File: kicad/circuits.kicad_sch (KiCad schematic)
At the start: 28 parts

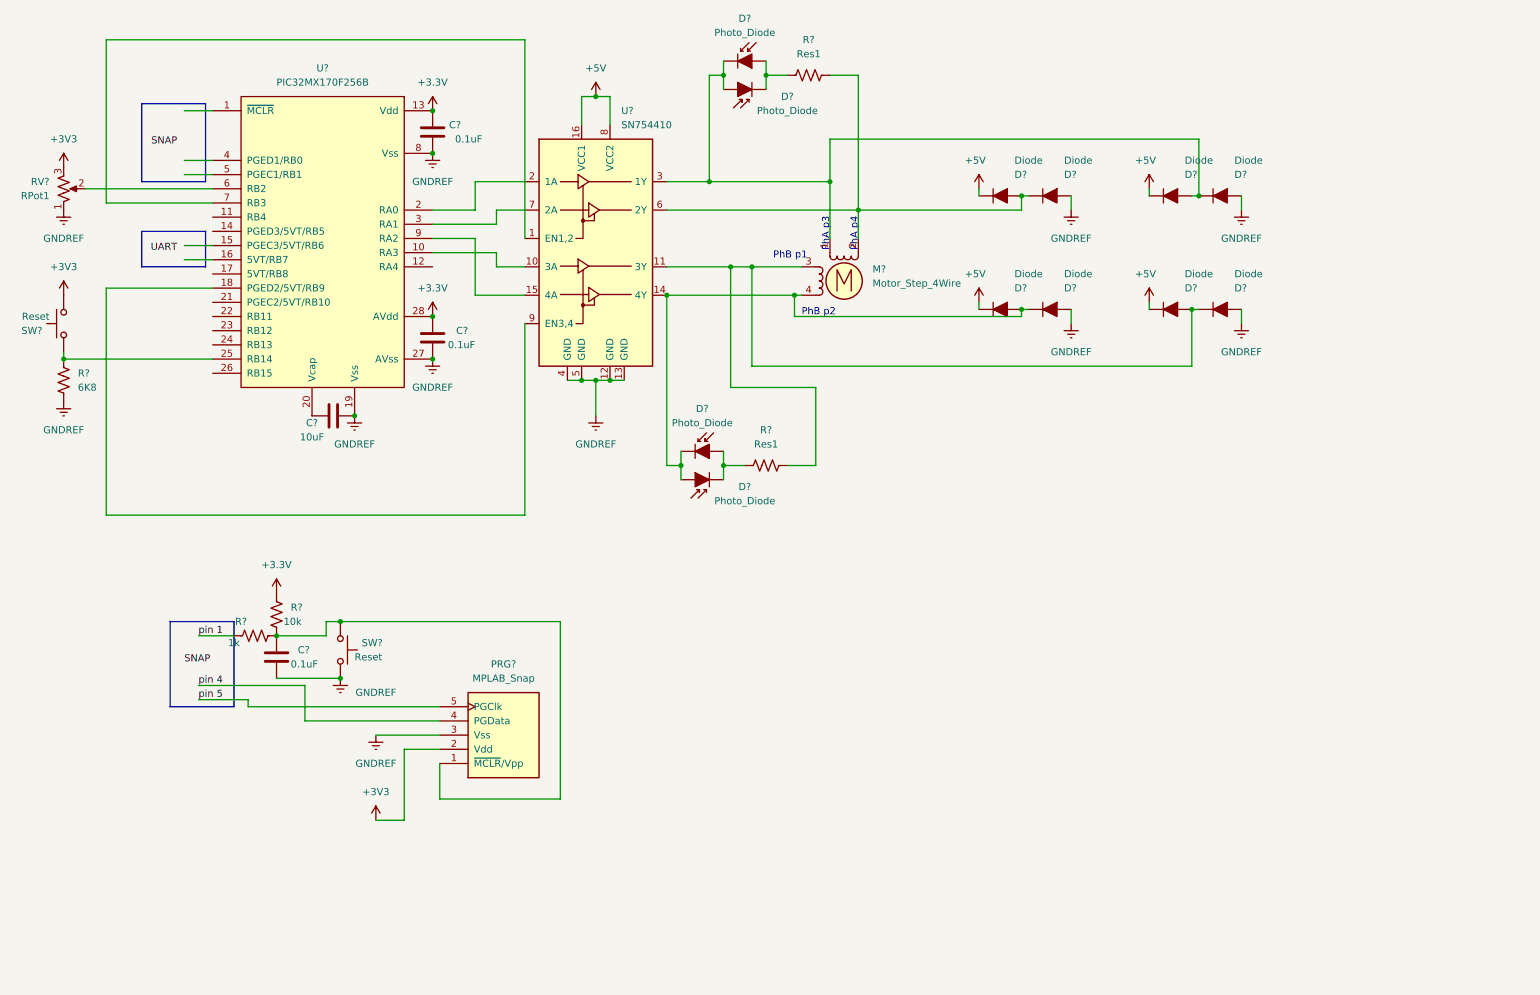
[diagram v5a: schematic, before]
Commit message: Modify lab 5 schematic for DC motor and nicer looks
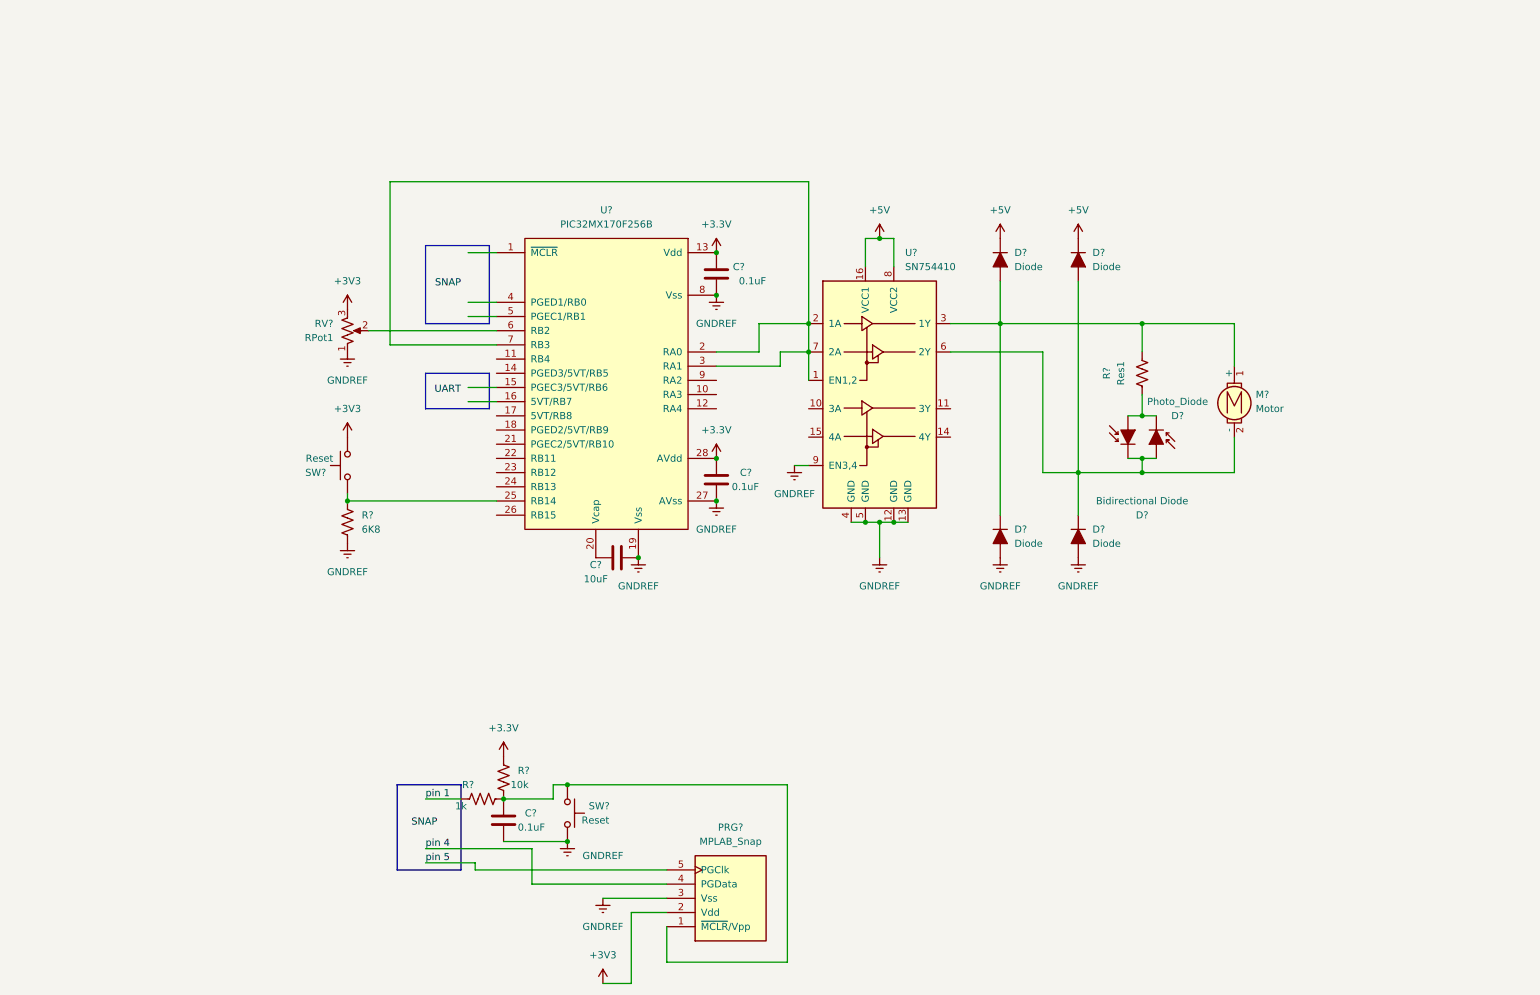
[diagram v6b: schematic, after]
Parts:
- removed D? (x2): Photo_Diode, symbol ME218_BaseLib:Photo_Diode
- removed D? (x8): Diode, symbol ME218_BaseLib:Diode
- removed M?: Motor_Step_4Wire, symbol ME218_BaseLib:Motor_Step_4Wire
- removed R?: Res1, symbol ME218_BaseLib:Res1
- added D? (x4): Diode, symbol 218:Diode
- added M?: Motor, symbol 218:Motor
- D?: value Photo_Diode -> Bidirectional Diode
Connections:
- net +5V: now also D?.1 (K), D?.1 (K)
- net GNDREF: now also U?.9 (EN3,4), D?.2 (A), D?.2 (A)
- net at U?.6 (2Y): now also D?.1 (K), D?.2 (A), D?.1 (K), D?.2 (A), M?.2 (-); no longer R?.2
- net at U?.10 (RA3): no longer U?.10 (3A)
- net at U?.18 (PGED2/5VT/RB9): no longer U?.9 (EN3,4)
- net at U?.2 (1A), U?.2 (RA0): now also U?.1 (EN1,2), U?.3 (RA1), U?.7 (2A), U?.7 (RB3)
- net at U?.9 (RA2): no longer U?.15 (4A)
- new net: D?.1 (K), D?.2 (A), M?.1 (+), R?.2, U?.3 (1Y)
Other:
- note removed: "PhA p3"
- note removed: "PhA p4"
- note removed: "PhB p1"
- note removed: "PhB p2"
- moved on the sheet: C?, D?, PRG?, R?, RV?, SW?, U?

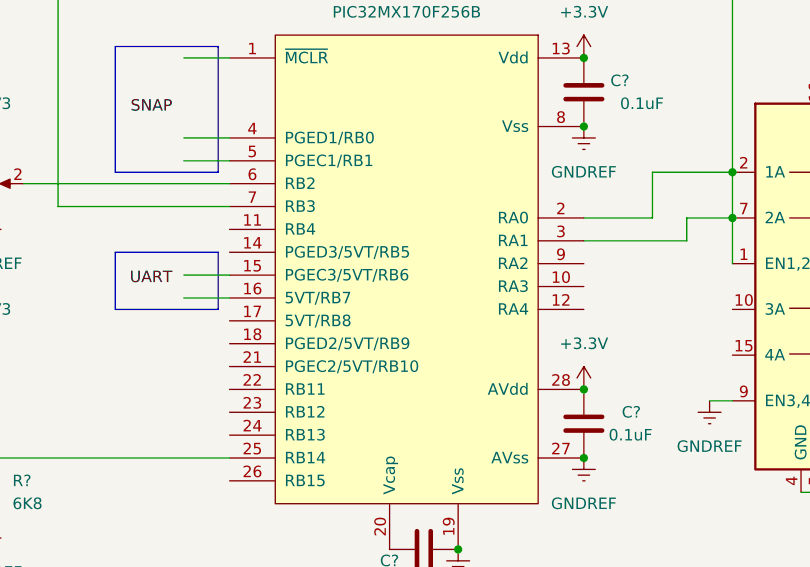
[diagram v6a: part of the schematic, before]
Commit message: Label IC/OC pins in schematic
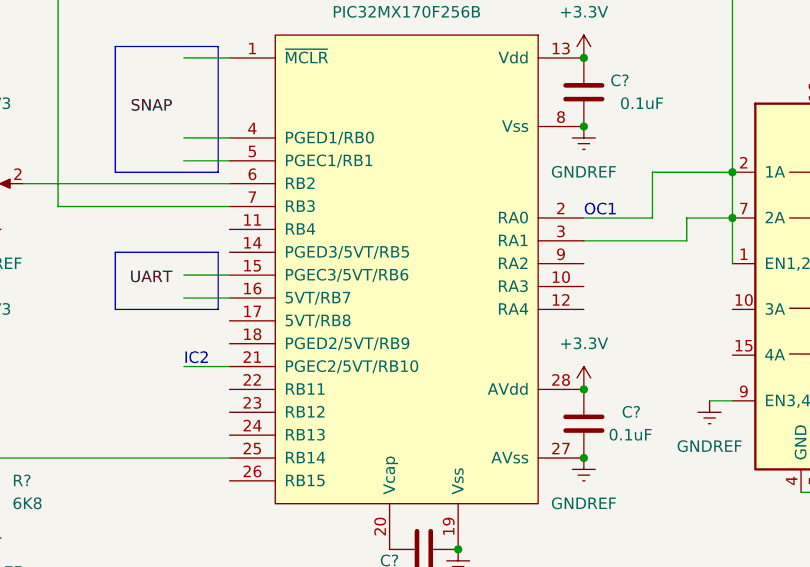
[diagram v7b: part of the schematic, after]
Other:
- note added: "IC2"
- note added: "OC1"
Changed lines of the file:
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@@
+    (stroke (width 0) (type default) (color 0 0 0 0))
+  )
+  (wire (pts (xy 93.98 91.44) (xy 99.06 91.44))
     (stroke (width 0) (type default) (color 0 0 0 0))
   )
@@
     (stroke (width 0) (type default) (color 0 0 0 0))
   )
+  (text "IC2" (at 93.98 91.44 0)
+    (effects (font (size 1.27 1.27)) (justify left bottom))
+  )
+  (text "OC1" (at 138.43 74.93 0)
+    (effects (font (size 1.27 1.27)) (justify left bottom))
+  )
   (label "pin 4" (at 86.36 163.83 0)

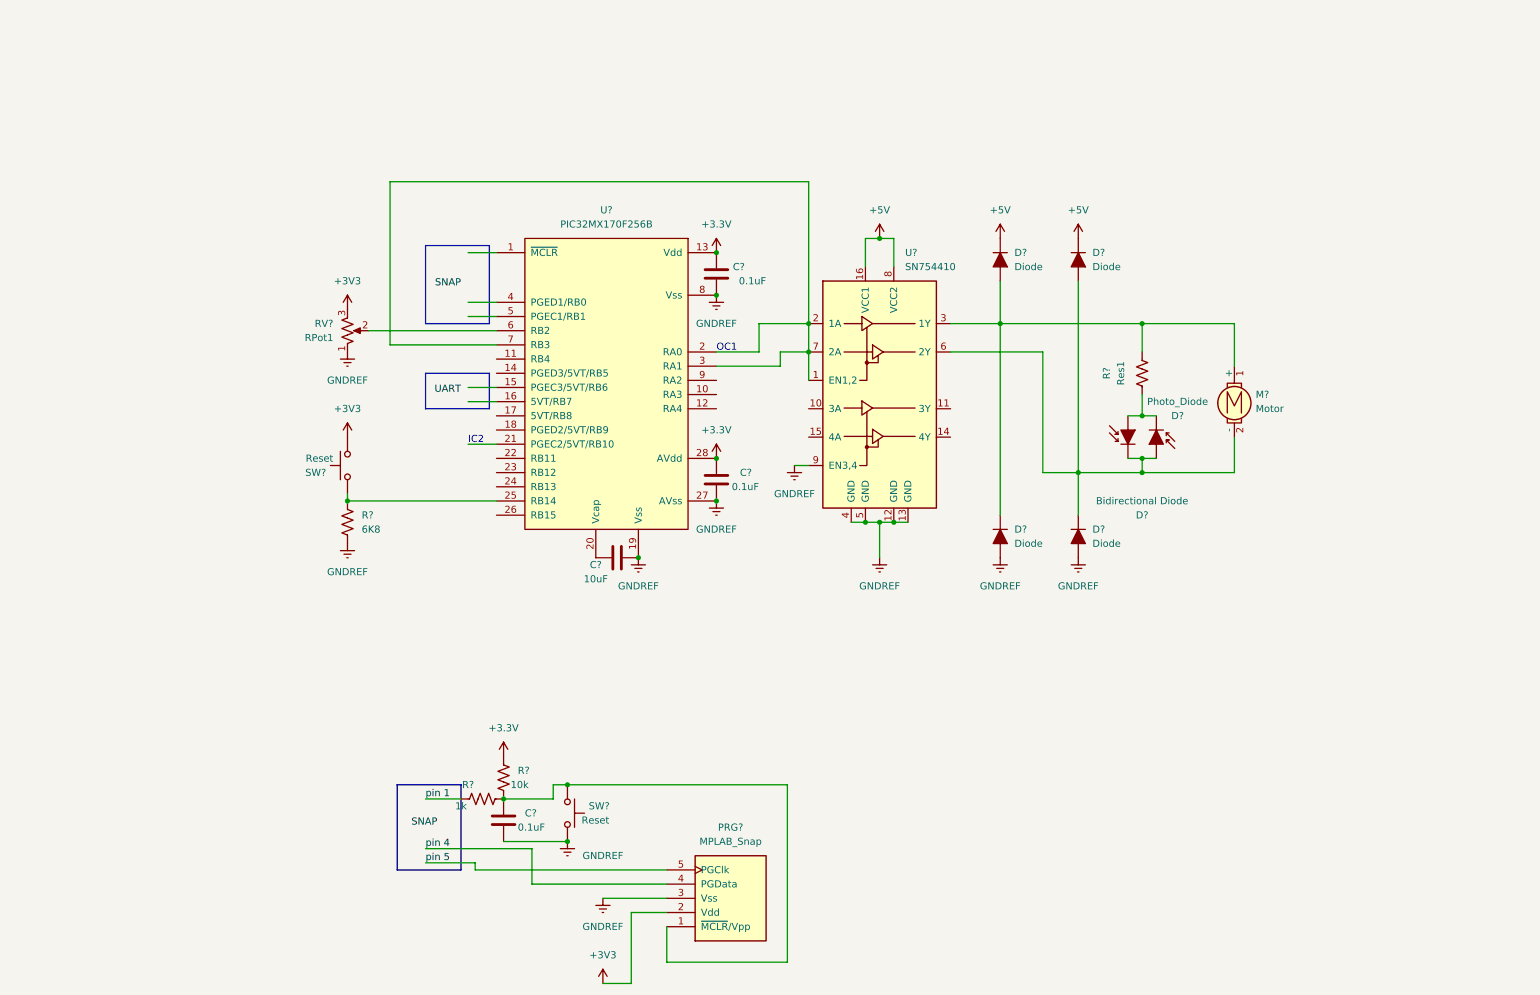
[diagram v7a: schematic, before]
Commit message: Add 8 bar LED control to schematic
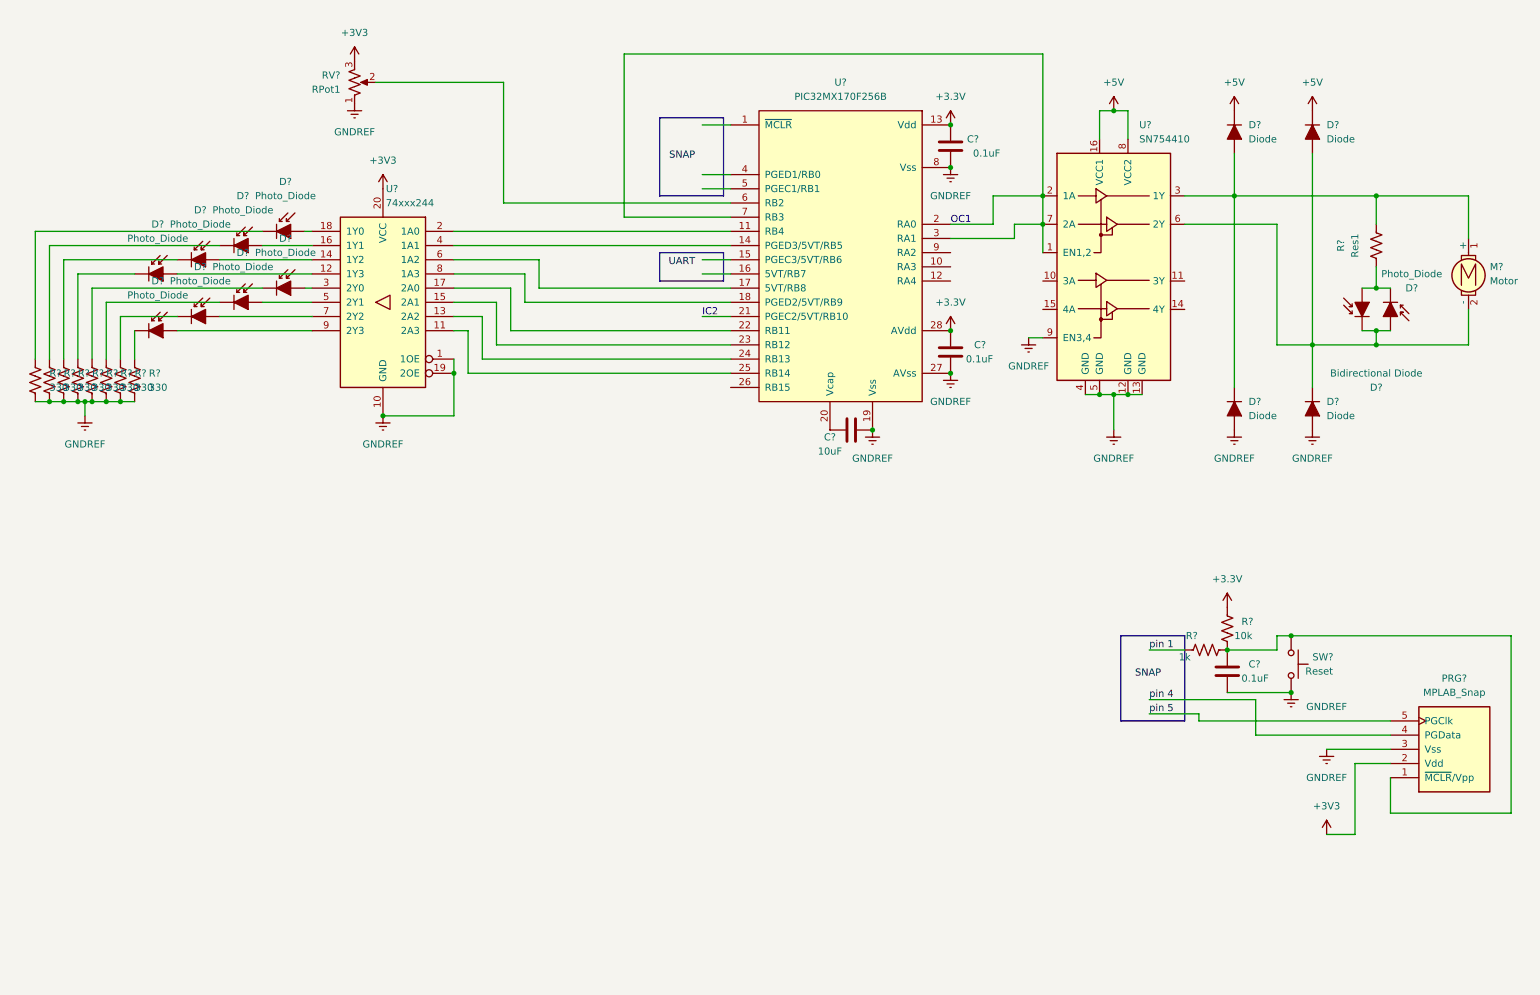
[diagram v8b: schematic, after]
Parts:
- removed R?: 6K8, symbol Device:R_US
- removed SW?: Reset, symbol ME218_BaseLib:SW-PB
- added D? (x8): Photo_Diode, symbol ME218_BaseLib:Photo_Diode
- added R? (x8): 330, symbol 218:Res1
- added U?: 74xxx244, symbol 218:74xxx244
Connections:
- net +3V3: now also U?.20 (VCC)
- net GNDREF: now also R?.2, R?.2, R?.2, R?.2, R?.2, R?.2, R?.2, R?.2, U?.1 (1OE), U?.10 (GND), U?.19 (2OE)
- net at U?.25 (RB14): now also U?.11 (2A3)
- net at U?.11 (RB4): now also U?.2 (1A0)
- net at U?.14 (PGED3/5VT/RB5): now also U?.4 (1A1)
- net at U?.17 (5VT/RB8): now also U?.6 (1A2)
- net at U?.18 (PGED2/5VT/RB9): now also U?.8 (1A3)
- net at U?.22 (RB11): now also U?.17 (2A0)
- net at U?.23 (RB12): now also U?.15 (2A1)
- net at U?.24 (RB13): now also U?.13 (2A2)
- new net: D?.1 (K), R?.1 (x8)
- new net: D?.2 (A), U?.12 (1Y3)
- new net: D?.2 (A), U?.14 (1Y2)
- new net: D?.2 (A), U?.16 (1Y1)
- new net: D?.2 (A), U?.7 (2Y2)
- new net: D?.2 (A), U?.3 (2Y0)
- new net: D?.2 (A), U?.9 (2Y3)
- new net: D?.2 (A), U?.18 (1Y0)
- new net: D?.2 (A), U?.5 (2Y1)
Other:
- moved on the sheet: C?, D?, M?, PRG?, R?, RV?, SW?, U?
